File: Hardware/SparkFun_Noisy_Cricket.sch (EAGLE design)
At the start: 28 parts, among them U1 LM4853

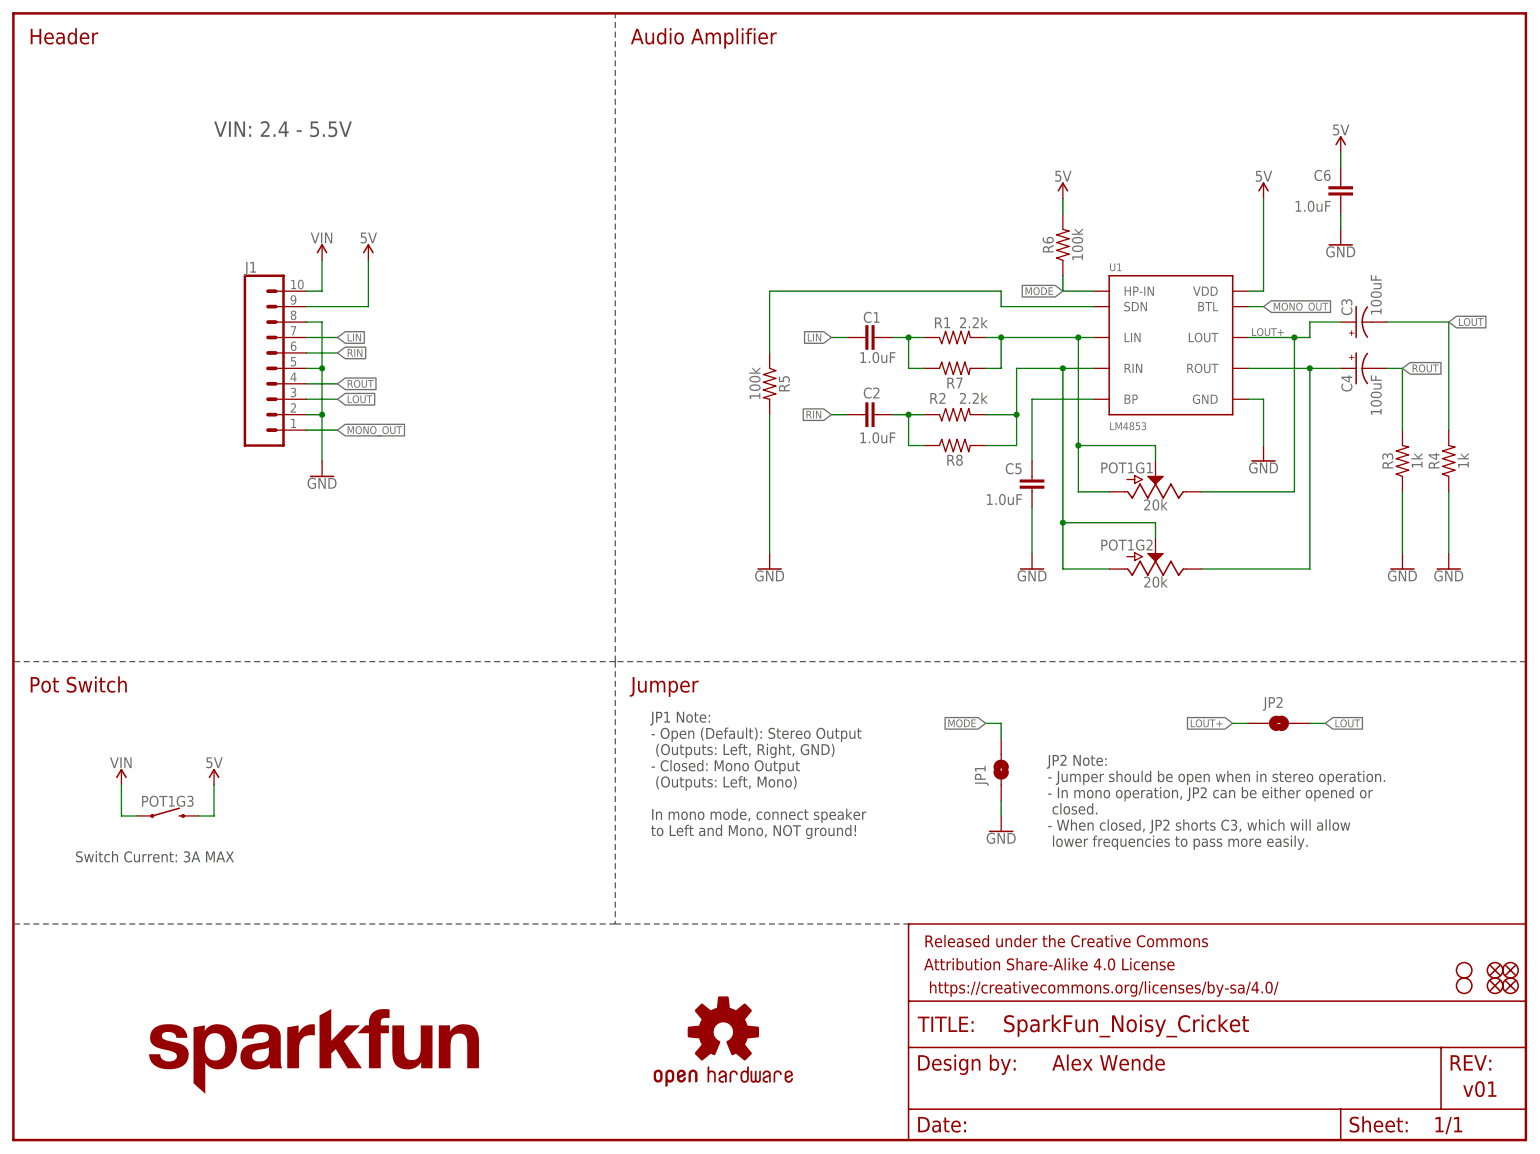
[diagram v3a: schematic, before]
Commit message: Design Review Changes
minor changes to silk after design review
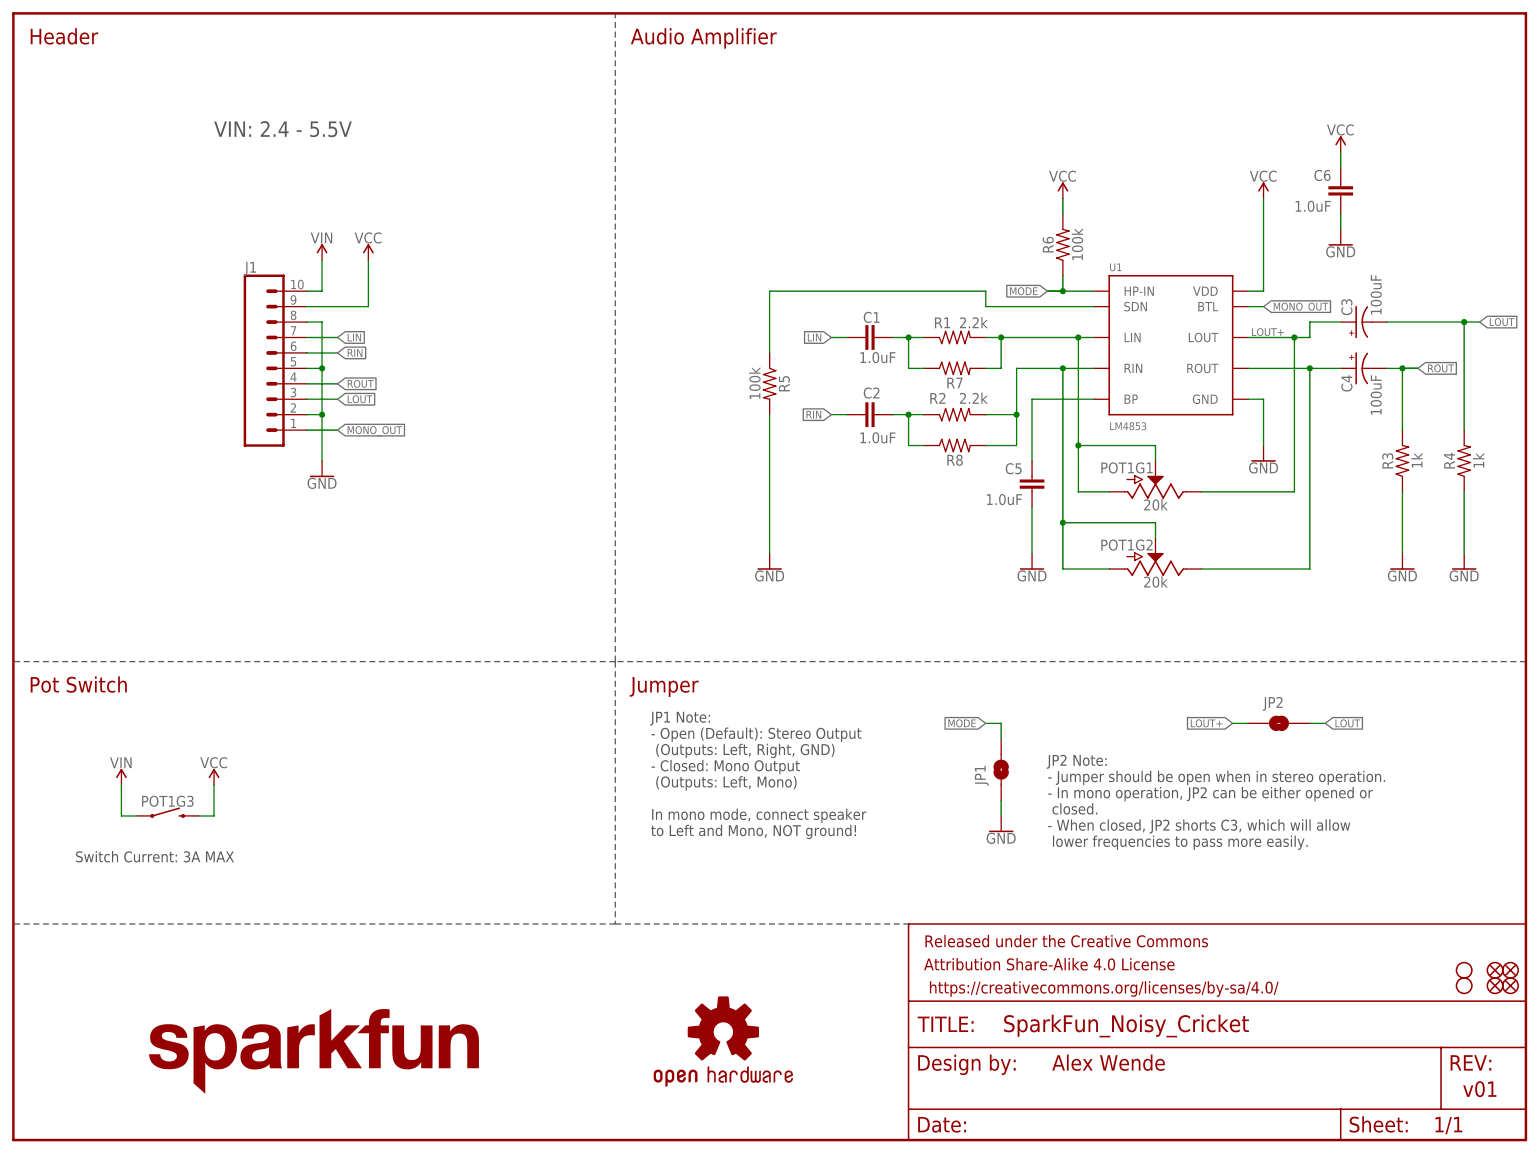
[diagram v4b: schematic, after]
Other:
- moved on the sheet: R4
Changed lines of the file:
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@@
 <part name="R5" library="SparkFun-Resistors" deviceset="100KOHM" device="-0603-1/10W-1%" value="100k"/>
 <part name="R6" library="SparkFun-Resistors" deviceset="100KOHM" device="-0603-1/10W-1%" value="100k"/>
-<part name="SUPPLY2" library="SparkFun-PowerSymbols" deviceset="5V" device=""/>
-<part name="SUPPLY3" library="SparkFun-PowerSymbols" deviceset="5V" device=""/>
+<part name="SUPPLY2" library="SparkFun-PowerSymbols" deviceset="VCC" device=""/>
+<part name="SUPPLY3" library="SparkFun-PowerSymbols" deviceset="VCC" device=""/>
 <part name="GND1" library="SparkFun-PowerSymbols" deviceset="GND" device=""/>
 <part name="GND2" library="SparkFun-PowerSymbols" deviceset="GND" device=""/>
@@
 <part name="GND6" library="SparkFun-PowerSymbols" deviceset="GND" device=""/>
 <part name="SUPPLY1" library="SparkFun-PowerSymbols" deviceset="VIN" device=""/>
-<part name="SUPPLY4" library="SparkFun-PowerSymbols" deviceset="5V" device=""/>
+<part name="SUPPLY4" library="SparkFun-PowerSymbols" deviceset="VCC" device=""/>
 <part name="SUPPLY5" library="SparkFun-PowerSymbols" deviceset="VIN" device=""/>
-<part name="SUPPLY6" library="SparkFun-PowerSymbols" deviceset="5V" device=""/>
+<part name="SUPPLY6" library="SparkFun-PowerSymbols" deviceset="VCC" device=""/>
 <part name="C6" library="SparkFun-Capacitors" deviceset="1.0UF" device="-0603-16V-10%-X7R" value="1.0uF"/>
 <part name="GND7" library="SparkFun-PowerSymbols" deviceset="GND" device=""/>
-<part name="SUPPLY7" library="SparkFun-PowerSymbols" deviceset="5V" device=""/>
+<part name="SUPPLY7" library="SparkFun-PowerSymbols" deviceset="VCC" device=""/>
 <part name="FD1" library="SparkFun-Aesthetics" deviceset="FIDUCIAL" device="UFIDUCIAL"/>
 <part name="FD2" library="SparkFun-Aesthetics" deviceset="FIDUCIAL" device="UFIDUCIAL"/>
@@
 <instance part="C4" gate="G$1" x="220.98" y="127" rot="MR270"/>
 <instance part="R3" gate="G$1" x="228.6" y="111.76" rot="R90"/>
-<instance part="R4" gate="G$1" x="236.22" y="111.76" rot="R90"/>
+<instance part="R4" gate="G$1" x="238.76" y="111.76" rot="R90"/>
 <instance part="R5" gate="G$1" x="124.46" y="124.46" rot="R270"/>
 <instance part="R6" gate="G$1" x="172.72" y="147.32" rot="R90"/>
@@
 <instance part="GND1" gate="1" x="205.74" y="111.76"/>
 <instance part="GND2" gate="1" x="228.6" y="93.98"/>
-<instance part="GND3" gate="1" x="236.22" y="93.98"/>
+<instance part="GND3" gate="1" x="238.76" y="93.98"/>
 <instance part="POT1" gate="G1" x="187.96" y="106.68" rot="MR90"/>
 <instance part="POT1" gate="G2" x="187.96" y="93.98" rot="MR90"/>
@@
 <pinref part="C3" gate="G$1" pin="-"/>
 <pinref part="R4" gate="G$1" pin="2"/>
-<wire x1="226.06" y1="134.62" x2="236.22" y2="134.62" width="0.1524" layer="91"/>
-<wire x1="236.22" y1="134.62" x2="236.22" y2="116.84" width="0.1524" layer="91"/>
-<label x="236.22" y="134.62" size="1.27" layer="95" xref="yes"/>
+<wire x1="226.06" y1="134.62" x2="238.76" y2="134.62" width="0.1524" layer="91"/>
+<wire x1="241.3" y1="134.62" x2="238.76" y2="134.62" width="0.1524" layer="91"/>
+<wire x1="238.76" y1="134.62" x2="238.76" y2="116.84" width="0.1524" layer="91"/>
+<label x="241.3" y="134.62" size="1.27" layer="95" xref="yes"/>
+<junction x="238.76" y="134.62"/>
 </segment>
 <segment>
@@
 <pinref part="R3" gate="G$1" pin="2"/>
 <wire x1="226.06" y1="127" x2="228.6" y2="127" width="0.1524" layer="91"/>
+<wire x1="228.6" y1="127" x2="231.14" y2="127" width="0.1524" layer="91"/>
+<wire x1="231.14" y1="127" x2="228.6" y2="127" width="0.1524" layer="91"/>
 <wire x1="228.6" y1="127" x2="228.6" y2="116.84" width="0.1524" layer="91"/>
-<label x="228.6" y="127" size="1.27" layer="95" xref="yes"/>
+<label x="231.14" y="127" size="1.27" layer="95" xref="yes"/>
+<junction x="228.6" y="127"/>
 </segment>
 <segment>
@@
 <pinref part="U1" gate="G$1" pin="SDN"/>
 <pinref part="R5" gate="G$1" pin="1"/>
-<wire x1="177.8" y1="137.16" x2="162.56" y2="137.16" width="0.1524" layer="91"/>
-<wire x1="162.56" y1="137.16" x2="162.56" y2="139.7" width="0.1524" layer="91"/>
-<wire x1="162.56" y1="139.7" x2="124.46" y2="139.7" width="0.1524" layer="91"/>
+<wire x1="177.8" y1="137.16" x2="160.02" y2="137.16" width="0.1524" layer="91"/>
+<wire x1="160.02" y1="137.16" x2="160.02" y2="139.7" width="0.1524" layer="91"/>
+<wire x1="160.02" y1="139.7" x2="124.46" y2="139.7" width="0.1524" layer="91"/>
 <wire x1="124.46" y1="139.7" x2="124.46" y2="129.54" width="0.1524" layer="91"/>
 </segment>
@@
 <pinref part="R6" gate="G$1" pin="2"/>
 <wire x1="172.72" y1="152.4" x2="172.72" y2="154.94" width="0.1524" layer="91"/>
-<pinref part="SUPPLY2" gate="G$1" pin="5V"/>
+<pinref part="SUPPLY2" gate="G$1" pin="VCC"/>
 </segment>
 <segment>
@@
 <wire x1="203.2" y1="139.7" x2="205.74" y2="139.7" width="0.1524" layer="91"/>
 <wire x1="205.74" y1="139.7" x2="205.74" y2="154.94" width="0.1524" layer="91"/>
-<pinref part="SUPPLY3" gate="G$1" pin="5V"/>
+<pinref part="SUPPLY3" gate="G$1" pin="VCC"/>
 </segment>
 <segment>
 <pinref part="J1" gate="G$1" pin="9"/>
-<pinref part="SUPPLY4" gate="G$1" pin="5V"/>
+<pinref part="SUPPLY4" gate="G$1" pin="VCC"/>
 <wire x1="48.26" y1="137.16" x2="58.42" y2="137.16" width="0.1524" layer="91"/>
 <wire x1="58.42" y1="137.16" x2="58.42" y2="144.78" width="0.1524" layer="91"/>
@@
 <wire x1="30.48" y1="53.34" x2="33.02" y2="53.34" width="0.1524" layer="91"/>
 <wire x1="33.02" y1="53.34" x2="33.02" y2="58.42" width="0.1524" layer="91"/>
-<pinref part="SUPPLY6" gate="G$1" pin="5V"/>
+<pinref part="SUPPLY6" gate="G$1" pin="VCC"/>
 </segment>
 <segment>
 <pinref part="C6" gate="G$1" pin="1"/>
 <wire x1="218.44" y1="160.02" x2="218.44" y2="162.56" width="0.1524" layer="91"/>
-<pinref part="SUPPLY7" gate="G$1" pin="5V"/>
+<pinref part="SUPPLY7" gate="G$1" pin="VCC"/>
 </segment>
 </net>
@@
 <segment>
 <pinref part="R4" gate="G$1" pin="1"/>
-<wire x1="236.22" y1="106.68" x2="236.22" y2="96.52" width="0.1524" layer="91"/>
+<wire x1="238.76" y1="106.68" x2="238.76" y2="96.52" width="0.1524" layer="91"/>
 <pinref part="GND3" gate="1" pin="GND"/>
 </segment>
@@
 <pinref part="R6" gate="G$1" pin="1"/>
 <wire x1="177.8" y1="139.7" x2="172.72" y2="139.7" width="0.1524" layer="91"/>
+<wire x1="172.72" y1="139.7" x2="170.18" y2="139.7" width="0.1524" layer="91"/>
+<wire x1="170.18" y1="139.7" x2="172.72" y2="139.7" width="0.1524" layer="91"/>
 <wire x1="172.72" y1="139.7" x2="172.72" y2="142.24" width="0.1524" layer="91"/>
-<label x="172.72" y="139.7" size="1.27" layer="95" rot="R180" xref="yes"/>
-</segment>
-<segment>
+<label x="170.18" y="139.7" size="1.27" layer="95" rot="R180" xref="yes"/>
+<junction x="172.72" y="139.7"/>
+</segment>
+<segment>

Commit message: QC Fixes
- Increased anular ring of pot from AUTO to 0.074".
- Fixed schematic version number to 10.
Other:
- note added: "v10"
- note removed: "v01"
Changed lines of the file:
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@@
 <text x="2.54" y="73.66" size="2.54" layer="94">Pot Switch</text>
 <text x="170.942" y="11.43" size="2.54" layer="94">Alex Wende</text>
-<text x="238.506" y="7.112" size="2.54" layer="94">v01</text>
+<text x="238.506" y="7.112" size="2.54" layer="94">v10</text>
 <text x="33.02" y="165.1" size="2.54" layer="97">VIN: 2.4 - 5.5V</text>
 <text x="10.16" y="45.72" size="1.778" layer="97">Switch Current: 3A MAX</text>
